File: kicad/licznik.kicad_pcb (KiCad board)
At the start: 2 copper layers, 54.6 x 45.7 mm, 32 parts, among them J1 Display, J2 Micro_SD_Card_Det, J3 Serial CS1, J4 Serial CS2, SW1 Wheel, SW2 Crank, SW3 Backlight, SW4 Right, SW5 Select, SW6 Left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

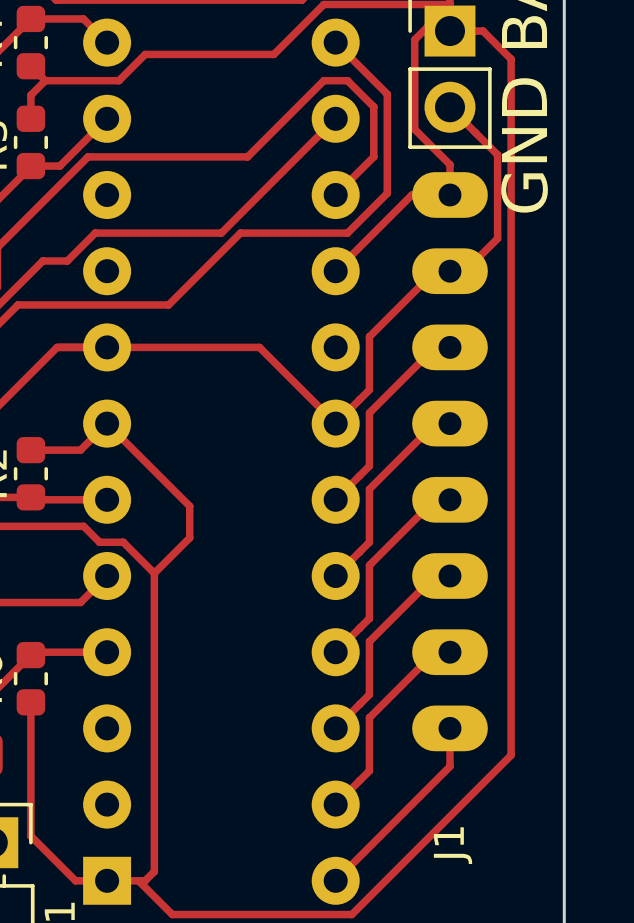
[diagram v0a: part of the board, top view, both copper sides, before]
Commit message: PCB footprint: Set screen holes to 1mm
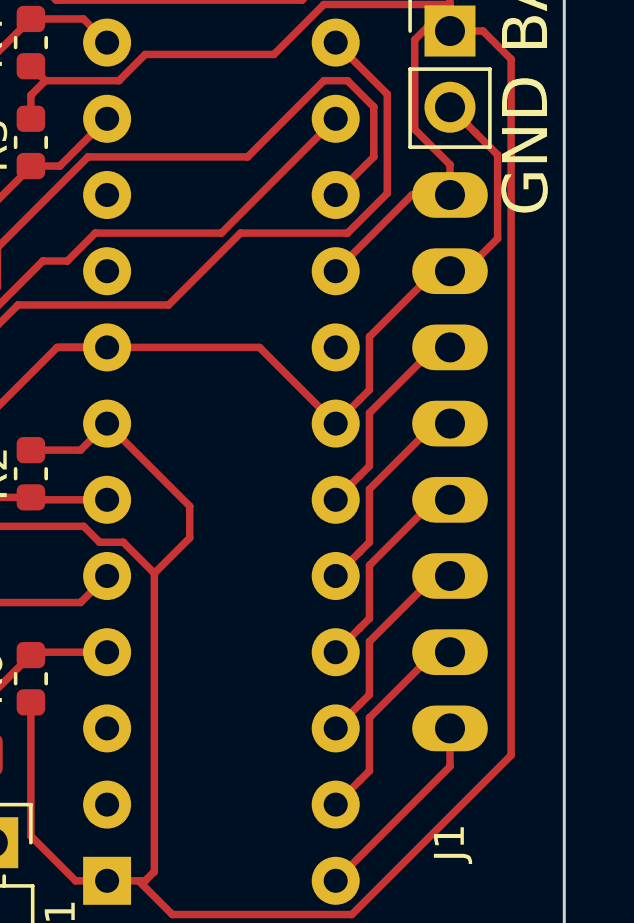
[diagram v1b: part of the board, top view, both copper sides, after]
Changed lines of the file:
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@@
-(kicad_pcb (version 20171130) (host pcbnew 5.0.1)
+(kicad_pcb (version 20171130) (host pcbnew 5.0.2)
   (general
     (thickness 1.6)
@@
     (uvia_drill 0.1)
   )
+  (module "Licznik:Nokia screen" (layer F.Cu)
+    (at 87.63 178.185622 270)
+    (fp_text reference J1 (at 12.7 0 270) (layer F.SilkS)
+      (effects (font (size 1 1) (thickness 0.15)))
+    )
+    (fp_text value Display (at 0 -3.81 270) (layer F.Fab)
+      (effects (font (size 1 1) (thickness 0.15)))
+    )
+    (fp_text user Nokia_pins2 (at 0 39.37 270) (layer F.Fab)
+      (effects (font (size 1 1) (thickness 0.15)))
+    )
+    (fp_line (start -8.89 40.64) (end 8.89 40.64) (layer F.Fab) (width 0.15))
+    (fp_circle (center 20.32 40.64) (end 20.32 39.37) (layer F.Fab) (width 0.15))
+    (fp_circle (center -20.32 40.64) (end -20.32 39.37) (layer F.Fab) (width 0.15))
+    (fp_circle (center -20.32 0) (end -20.32 -1.27) (layer F.Fab) (width 0.15))
+    (fp_circle (center 20.32 0) (end 21.59 0) (layer F.Fab) (width 0.15))
+    (fp_line (start 22.5 42.46) (end 22.5 -2.54) (layer F.Fab) (width 0.15))
+    (fp_line (start -22.5 42.46) (end 22.5 42.46) (layer F.Fab) (width 0.15))
+    (fp_line (start -22.5 42.46) (end -22.5 -2.54) (layer F.Fab) (width 0.15))
+    (fp_line (start -22.5 -2.54) (end 22.5 -2.54) (layer F.Fab) (width 0.15))
+    (fp_text user GND (at -6.35 3.81 180) (layer F.Fab)
+      (effects (font (size 1 1) (thickness 0.15)))
+    )
+    (fp_text user VCC (at -8.89 3.81 180) (layer F.Fab)
+      (effects (font (size 1 1) (thickness 0.15)))
+    )
+    (pad 8 thru_hole oval (at 8.89 0 270) (size 1.524 2.524) (drill 1) (layers *.Cu *.Mask)
+      (net 10 "Net-(J1-Pad8)"))
+    (pad 7 thru_hole oval (at 6.35 0 270) (size 1.524 2.524) (drill 1) (layers *.Cu *.Mask)
+      (net 9 "Net-(J1-Pad7)"))
+    (pad 6 thru_hole oval (at 3.81 0 270) (size 1.524 2.524) (drill 1) (layers *.Cu *.Mask)
+      (net 8 "Net-(J1-Pad6)"))
+    (pad 5 thru_hole oval (at 1.27 0 270) (size 1.524 2.524) (drill 1) (layers *.Cu *.Mask)
+      (net 7 "Net-(J1-Pad5)"))
+    (pad 4 thru_hole oval (at -1.27 0 270) (size 1.524 2.524) (drill 1) (layers *.Cu *.Mask)
+      (net 6 "Net-(J1-Pad4)"))
+    (pad 3 thru_hole oval (at -3.81 0 270) (size 1.524 2.524) (drill 1) (layers *.Cu *.Mask)
+      (net 5 "Net-(J1-Pad3)"))
+    (pad 2 thru_hole oval (at -6.35 0 270) (size 1.524 2.524) (drill 1) (layers *.Cu *.Mask)
+      (net 24 GND))
+    (pad 1 thru_hole oval (at -8.89 0 270) (size 1.524 2.524) (drill 1) (layers *.Cu *.Mask)
+      (net 22 +BATT))
+  )
   (module MountingHole:MountingHole_2.5mm (layer F.Cu)
     (at 46.99 157.855)
@@
     )
     (pad 1 np_thru_hole circle (at 0 0) (size 2.5 2.5) (drill 2.5) (layers *.Cu *.Mask))
-  )
-  (module "Licznik:Nokia screen" (layer F.Cu)
-    (at 87.63 178.185622 270)
-    (fp_text reference J1 (at 12.7 0 270) (layer F.SilkS)
-      (effects (font (size 1 1) (thickness 0.15)))
-    )
-    (fp_text value Display (at 0 -3.81 270) (layer F.Fab)
-      (effects (font (size 1 1) (thickness 0.15)))
-    )
-    (fp_text user VCC (at -8.89 3.81 180) (layer F.Fab)
-      (effects (font (size 1 1) (thickness 0.15)))
-    )
-    (fp_text user GND (at -6.35 3.81 180) (layer F.Fab)
-      (effects (font (size 1 1) (thickness 0.15)))
-    )
-    (fp_line (start -22.5 -2.54) (end 22.5 -2.54) (layer F.Fab) (width 0.15))
-    (fp_line (start -22.5 42.46) (end -22.5 -2.54) (layer F.Fab) (width 0.15))
-    (fp_line (start -22.5 42.46) (end 22.5 42.46) (layer F.Fab) (width 0.15))
-    (fp_line (start 22.5 42.46) (end 22.5 -2.54) (layer F.Fab) (width 0.15))
-    (fp_circle (center 20.32 0) (end 21.59 0) (layer F.Fab) (width 0.15))
-    (fp_circle (center -20.32 0) (end -20.32 -1.27) (layer F.Fab) (width 0.15))
-    (fp_circle (center -20.32 40.64) (end -20.32 39.37) (layer F.Fab) (width 0.15))
-    (fp_circle (center 20.32 40.64) (end 20.32 39.37) (layer F.Fab) (width 0.15))
-    (fp_line (start -8.89 40.64) (end 8.89 40.64) (layer F.Fab) (width 0.15))
-    (fp_text user Nokia_pins2 (at 0 39.37 270) (layer F.Fab)
-      (effects (font (size 1 1) (thickness 0.15)))
-    )
-    (pad 1 thru_hole oval (at -8.89 0 270) (size 1.524 2.524) (drill 0.762) (layers *.Cu *.Mask)
-      (net 22 +BATT))
-    (pad 2 thru_hole oval (at -6.35 0 270) (size 1.524 2.524) (drill 0.762) (layers *.Cu *.Mask)
-      (net 24 GND))
-    (pad 3 thru_hole oval (at -3.81 0 270) (size 1.524 2.524) (drill 0.762) (layers *.Cu *.Mask)
-      (net 5 "Net-(J1-Pad3)"))
-    (pad 4 thru_hole oval (at -1.27 0 270) (size 1.524 2.524) (drill 0.762) (layers *.Cu *.Mask)
-      (net 6 "Net-(J1-Pad4)"))
-    (pad 5 thru_hole oval (at 1.27 0 270) (size 1.524 2.524) (drill 0.762) (layers *.Cu *.Mask)
-      (net 7 "Net-(J1-Pad5)"))
-    (pad 6 thru_hole oval (at 3.81 0 270) (size 1.524 2.524) (drill 0.762) (layers *.Cu *.Mask)
-      (net 8 "Net-(J1-Pad6)"))
-    (pad 7 thru_hole oval (at 6.35 0 270) (size 1.524 2.524) (drill 0.762) (layers *.Cu *.Mask)
-      (net 9 "Net-(J1-Pad7)"))
-    (pad 8 thru_hole oval (at 8.89 0 270) (size 1.524 2.524) (drill 0.762) (layers *.Cu *.Mask)
-      (net 10 "Net-(J1-Pad8)"))
   )
   (module Resistor_SMD:R_0603_1608Metric (layer F.Cu)
@@
       (effects (font (size 0.5 0.5) (thickness 0.08)))
     )
-    (pad 1 smd roundrect (at -0.9375 0 315) (size 0.975 1.4) (layers F.Cu F.Paste F.Mask) (roundrect_rratio 0.25)
+    (pad 1 smd roundrect (at -0.937501 0 315) (size 0.975 1.4) (layers F.Cu F.Paste F.Mask) (roundrect_rratio 0.25)
       (net 12 "Net-(C5-Pad1)"))
-    (pad 2 smd roundrect (at 0.9375 0 315) (size 0.975 1.4) (layers F.Cu F.Paste F.Mask) (roundrect_rratio 0.25)
+    (pad 2 smd roundrect (at 0.937501 0 315) (size 0.975 1.4) (layers F.Cu F.Paste F.Mask) (roundrect_rratio 0.25)
       (net 24 GND))
     (model ${KISYS3DMOD}/Capacitor_SMD.3dshapes/C_0805_2012Metric.wrl

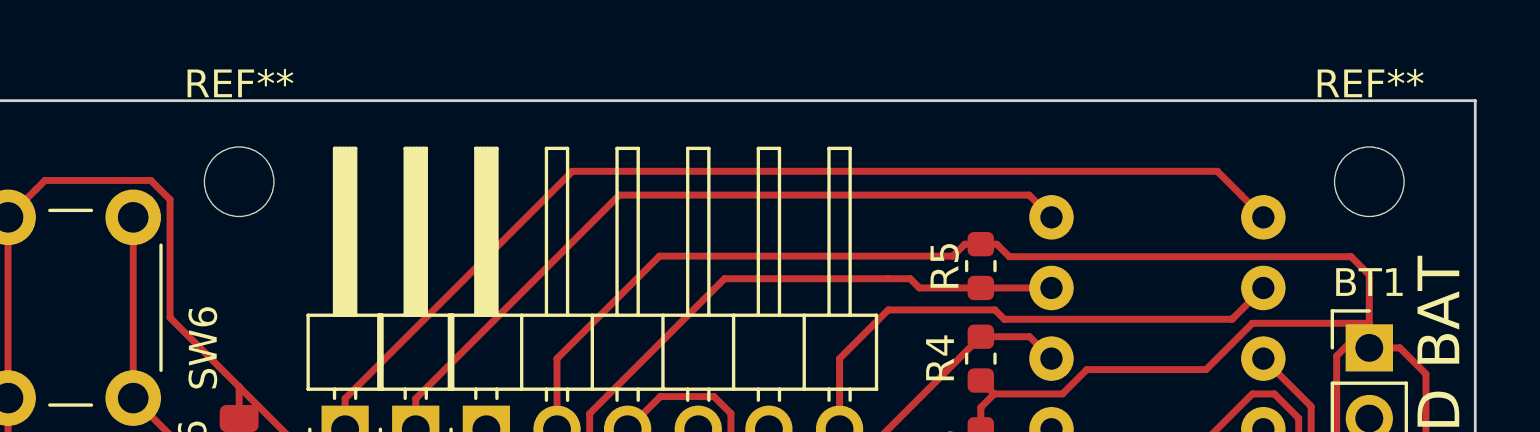
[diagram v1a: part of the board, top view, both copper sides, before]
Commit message: PCB: Adjust position of screen mounting holes
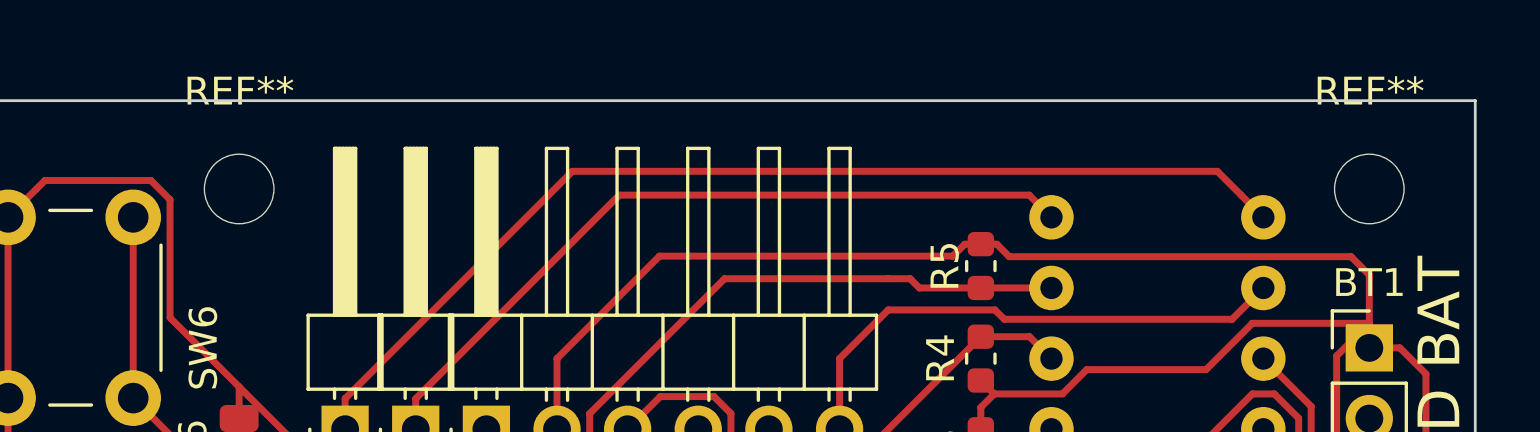
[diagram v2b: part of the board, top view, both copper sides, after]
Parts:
- removed the REF** at (47.0, 157.9)
- removed the REF** at (87.6, 157.9)
- added REF**: MountingHole_2.5mm, MountingHole:MountingHole_2.5mm, F.Cu at (47.0, 158.1)
- added REF**: MountingHole_2.5mm, MountingHole:MountingHole_2.5mm, F.Cu at (87.6, 158.1)
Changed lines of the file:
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@@
   )
   (module MountingHole:MountingHole_2.5mm (layer F.Cu)
-    (at 46.99 157.855)
+    (at 46.99 158.115)
     (descr "Mounting Hole 2.5mm, no annular")
     (tags "mounting hole 2.5mm no annular")
@@
   )
   (module MountingHole:MountingHole_2.5mm (layer F.Cu)
-    (at 87.63 157.855)
+    (at 87.63 158.115)
     (descr "Mounting Hole 2.5mm, no annular")
     (tags "mounting hole 2.5mm no annular")

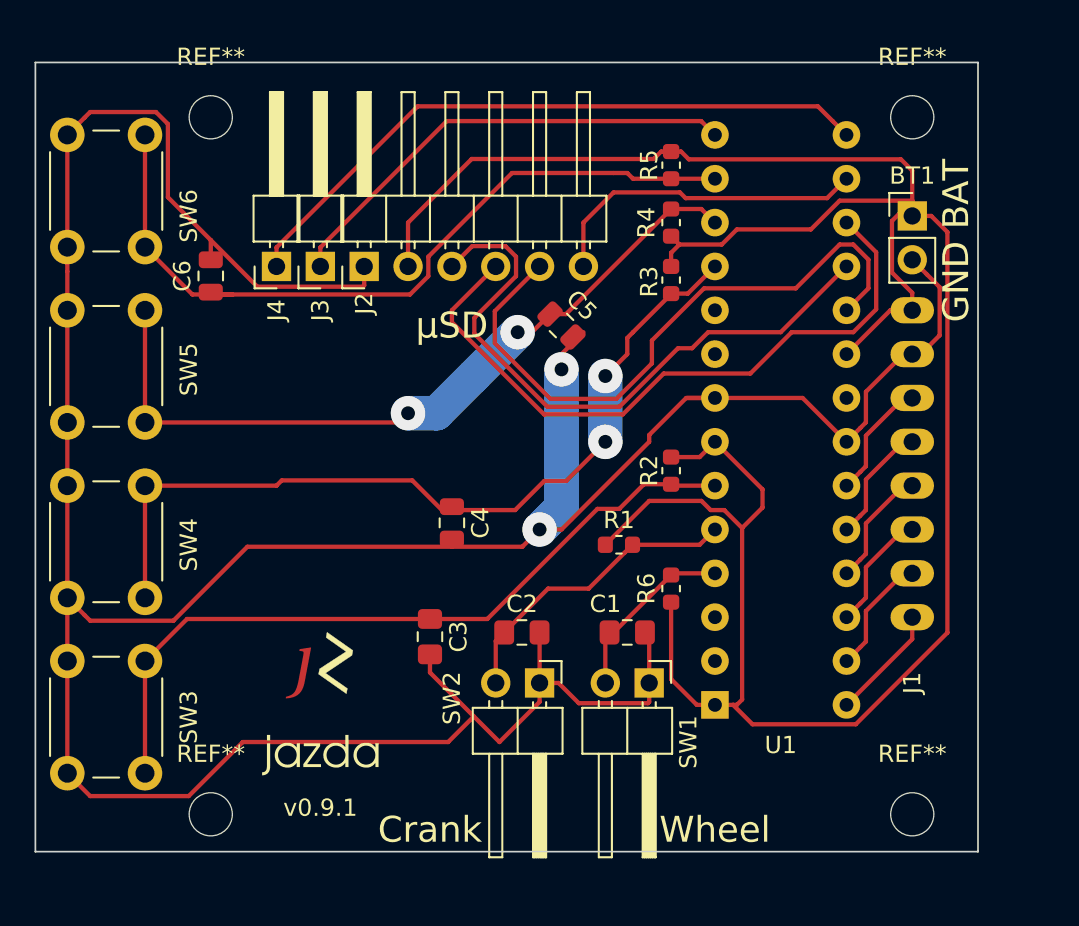
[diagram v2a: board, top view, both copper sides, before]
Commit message: PCB: Fix screen hole placement, reduce board size
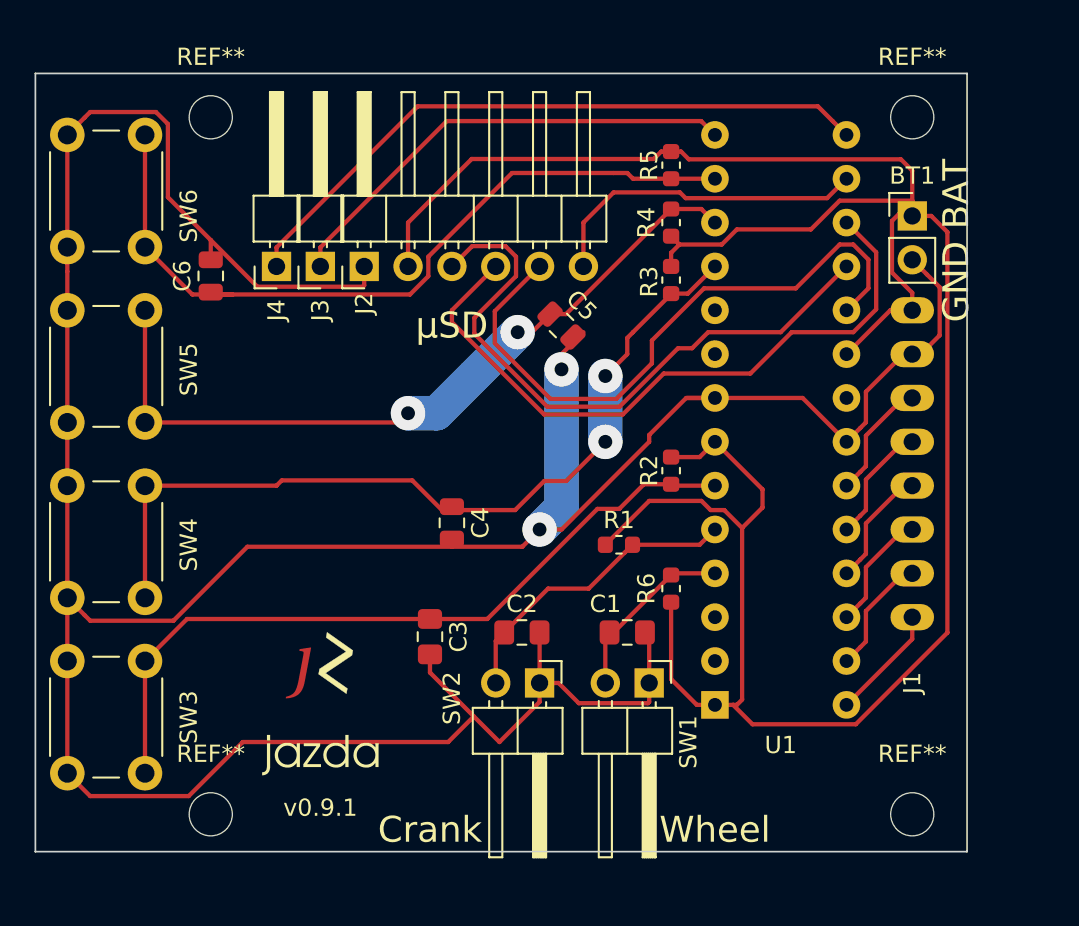
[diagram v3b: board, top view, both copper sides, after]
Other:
- board size 54.6 x 45.7 mm -> 54 x 45.1 mm
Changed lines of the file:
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@@
   (general
     (thickness 1.6)
-    (drawings 18)
+    (drawings 17)
     (tracks 267)
     (zones 0)
@@
       (effects (font (size 1 1) (thickness 0.15)))
     )
+    (fp_circle (center 0 0) (end 2.75 0) (layer F.CrtYd) (width 0.05))
+    (fp_circle (center 0 0) (end 2.5 0) (layer Cmts.User) (width 0.15))
     (fp_text user %R (at 0.3 0) (layer F.Fab)
       (effects (font (size 1 1) (thickness 0.15)))
     )
-    (fp_circle (center 0 0) (end 2.5 0) (layer Cmts.User) (width 0.15))
-    (fp_circle (center 0 0) (end 2.75 0) (layer F.CrtYd) (width 0.05))
     (pad 1 np_thru_hole circle (at 0 0) (size 2.5 2.5) (drill 2.5) (layers *.Cu *.Mask))
   )
@@
     (effects (font (size 1.5 1.5) (thickness 0.3)) (justify mirror))
   )
-  (dimension 45.72 (width 0.3) (layer Cmts.User)
-    (gr_text "45.720 mm" (at 30.92 177.8 270) (layer Cmts.User)
+  (dimension 45.085 (width 0.3) (layer Cmts.User)
+    (gr_text "45.085 mm" (at 30.92 178.1175 270) (layer Cmts.User)
       (effects (font (size 1.5 1.5) (thickness 0.3)))
     )
     (feature1 (pts (xy 36.83 200.66) (xy 32.433579 200.66)))
-    (feature2 (pts (xy 36.83 154.94) (xy 32.433579 154.94)))
-    (crossbar (pts (xy 33.02 154.94) (xy 33.02 200.66)))
+    (feature2 (pts (xy 36.83 155.575) (xy 32.433579 155.575)))
+    (crossbar (pts (xy 33.02 155.575) (xy 33.02 200.66)))
     (arrow1a (pts (xy 33.02 200.66) (xy 32.433579 199.533496)))
     (arrow1b (pts (xy 33.02 200.66) (xy 33.606421 199.533496)))
-    (arrow2a (pts (xy 33.02 154.94) (xy 32.433579 156.066504)))
-    (arrow2b (pts (xy 33.02 154.94) (xy 33.606421 156.066504)))
-  )
-  (dimension 54.61 (width 0.3) (layer Cmts.User)
-    (gr_text "54.610 mm" (at 64.135 150.3) (layer Cmts.User)
+    (arrow2a (pts (xy 33.02 155.575) (xy 32.433579 156.701504)))
+    (arrow2b (pts (xy 33.02 155.575) (xy 33.606421 156.701504)))
+  )
+  (dimension 53.975074 (width 0.3) (layer Cmts.User)
+    (gr_text "53.975 mm" (at 63.792377 150.960325 -0.09459659947) (layer Cmts.User)
       (effects (font (size 1.5 1.5) (thickness 0.3)))
     )
-    (feature1 (pts (xy 36.83 154.94) (xy 36.83 151.813579)))
-    (feature2 (pts (xy 91.44 154.94) (xy 91.44 151.813579)))
-    (crossbar (pts (xy 91.44 152.4) (xy 36.83 152.4)))
-    (arrow1a (pts (xy 36.83 152.4) (xy 37.956504 151.813579)))
-    (arrow1b (pts (xy 36.83 152.4) (xy 37.956504 152.986421)))
-    (arrow2a (pts (xy 91.44 152.4) (xy 90.313496 151.813579)))
-    (arrow2b (pts (xy 91.44 152.4) (xy 90.313496 152.986421)))
-  )
-  (target plus (at 100.33 195.965622) (size 5) (width 0.1) (layer Edge.Cuts))
+    (feature1 (pts (xy 36.797364 155.466648) (xy 36.802379 152.429345)))
+    (feature2 (pts (xy 90.772364 155.555762) (xy 90.777379 152.518459)))
+    (crossbar (pts (xy 90.77641 153.104879) (xy 36.80141 153.015765)))
+    (arrow1a (pts (xy 36.80141 153.015765) (xy 37.92888 152.431205)))
+    (arrow1b (pts (xy 36.80141 153.015765) (xy 37.926944 153.604045)))
+    (arrow2a (pts (xy 90.77641 153.104879) (xy 89.650876 152.516599)))
+    (arrow2b (pts (xy 90.77641 153.104879) (xy 89.64894 153.689439)))
+  )
   (gr_text CS2 (at 50.8 157.48 270) (layer B.SilkS)
     (effects (font (size 1.5 1.5) (thickness 0.3)) (justify mirror))
@@
     (effects (font (size 1.5 1.5) (thickness 0.3)))
   )
-  (gr_line (start 91.44 200.66) (end 91.44 154.94) (angle 90) (layer Edge.Cuts) (width 0.1))
-  (gr_line (start 36.83 154.94) (end 91.44 154.94) (angle 90) (layer Edge.Cuts) (width 0.1))
-  (gr_line (start 36.83 200.66) (end 36.83 154.94) (angle 90) (layer Edge.Cuts) (width 0.1))
-  (gr_line (start 36.83 200.66) (end 91.44 200.66) (angle 90) (layer Edge.Cuts) (width 0.1))
+  (gr_line (start 90.805 200.66) (end 90.805 155.575) (angle 90) (layer Edge.Cuts) (width 0.1))
+  (gr_line (start 36.83 155.575) (end 90.805 155.575) (angle 90) (layer Edge.Cuts) (width 0.1))
+  (gr_line (start 36.83 200.66) (end 36.83 155.575) (angle 90) (layer Edge.Cuts) (width 0.1))
+  (gr_line (start 36.83 200.66) (end 90.805 200.66) (angle 90) (layer Edge.Cuts) (width 0.1))
   (segment (start 69.85 188.205) (end 70.095 187.96) (width 0.25) (layer F.Cu) (net 1))
   (segment (start 69.85 190.885622) (end 69.85 188.205) (width 0.25) (layer F.Cu) (net 1))
